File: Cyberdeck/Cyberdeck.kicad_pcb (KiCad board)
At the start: 4 copper layers, 66 parts, among them SW1 Slide Switch, SW10 Push Button, SW11 Push Button, SW2 Push Button, SW3 Push Button, SW4 Push Button, SW5 Push Button, SW6 Push Button, SW7 Push Button, SW8 Push Button, SW9 Push Button, U1 18650 Positive Clip, U2 BQ24075 Charger, U3 0.47uH, U4 TPS62827 Regulator, U5 STM32F411CEU6, X1 32.768KHz 12.5pF, X2 25MHZ 12PF 10PPM

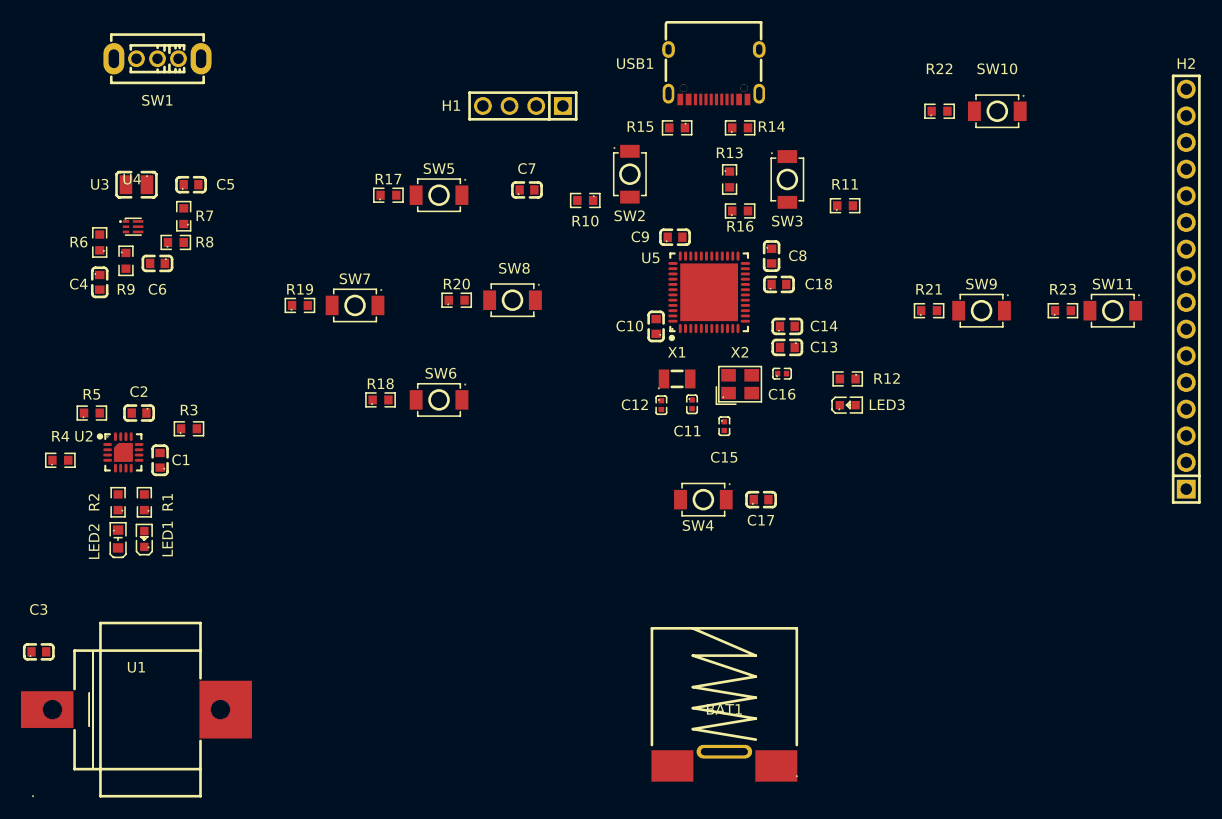
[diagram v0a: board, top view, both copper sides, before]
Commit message: Optimized component placement
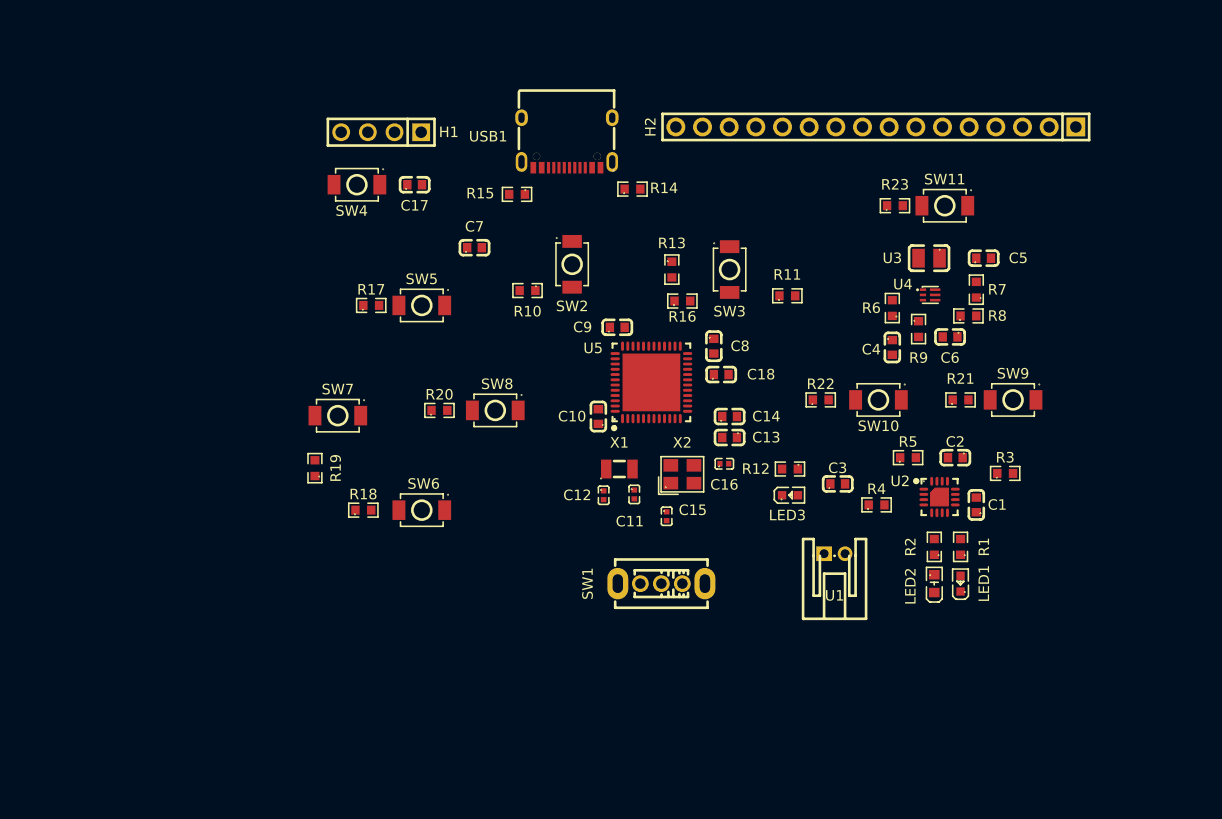
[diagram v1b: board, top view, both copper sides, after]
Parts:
- removed BAT1: 18650 Neg Clip, lcsc_footprints:C19184124_BAT-TH_MY-18650-05-J
- U1: value 18650 Positive Clip -> JST-PH BAT; footprint lcsc_footprints:C2979182_BAT-SMD_MY-18650-02 -> lcsc_footprints:C173752_CONN-TH_S2B-PH-K-S-LF-SN
- moved C1 77.9 mm to (181.5, 110.0)
- moved C2 77.9 mm to (179.5, 105.5)
- moved LED1 77.9 mm to (180.0, 117.5)
- moved LED2 77.9 mm to (177.5, 117.5)
- moved R1 77.9 mm to (180.0, 114.0)
- moved R2 77.9 mm to (177.5, 114.0)
- moved R3 77.9 mm to (184.2, 107.0)
- moved R4 77.9 mm to (172.0, 110.0)
- moved R5 77.9 mm to (175.0, 105.5)
- moved U2 77.9 mm to (178.0, 109.2)
- moved C3 77.8 mm to (168.3, 108.0)
- moved U4 76.2 mm to (177.0, 90.0)
- moved C6 75.8 mm to (179.0, 94.0)
- moved R7 75.8 mm to (181.5, 89.5)
- moved R8 75.8 mm to (180.8, 92.0)
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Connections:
- U1 pad 1: /V_BAT -> GND

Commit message: Routed all connections
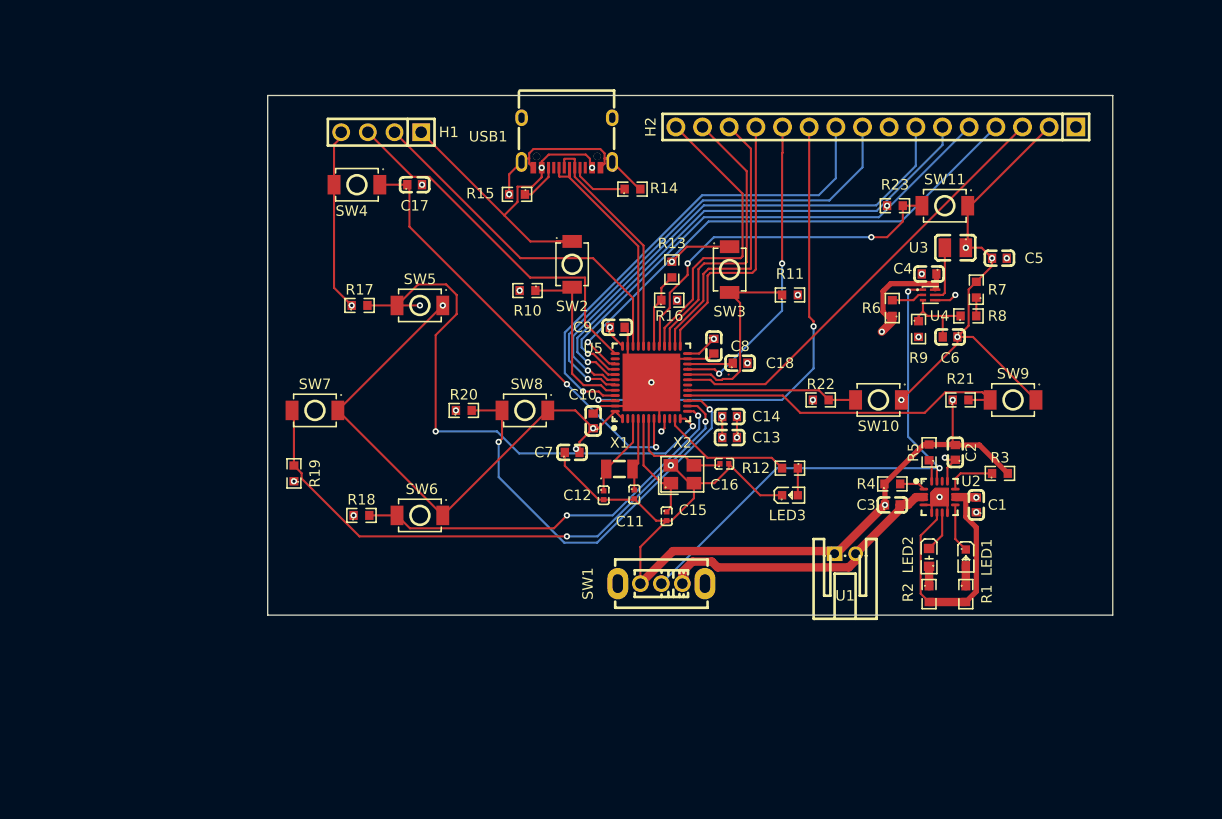
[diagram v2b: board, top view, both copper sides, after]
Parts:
- moved C7 21.6 mm to (143.0, 105.0)
- moved C4 7.83 mm to (177.0, 88.0), turned to 180 degrees
- moved C3 5.57 mm to (173.5, 110.0)
- moved R1 4.53 mm to (180.5, 118.5), turned to -90 degrees
- moved R2 4.53 mm to (177.0, 118.5), turned to -90 degrees
- moved SW8 2.82 mm to (138.5, 101.0)
- moved U3 2.69 mm to (179.5, 85.5)
- moved LED1 2.55 mm to (180.5, 115.0), turned to -90 degrees
- moved LED2 2.55 mm to (177.0, 115.0), turned to 90 degrees
- moved R4 2.50 mm to (173.5, 108.0)
- moved R20 2.32 mm to (132.7, 101.0)
- moved SW7 2.24 mm to (118.5, 101.0)
- moved C18 2.10 mm to (159.0, 96.5)
- moved R19 2.06 mm to (116.5, 107.0)
- moved R5 2.06 mm to (177.0, 105.0), turned to 90 degrees
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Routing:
- net GND: track 0.00 -> 468.2 mm, vias 0 -> 24
- net /V_IN: track 0.00 -> 334.7 mm, vias 0 -> 16
- net /V_CHG: track 0.00 -> 59.9 mm, vias 0 -> 2
- net /LEFT: track 0.00 -> 55.3 mm, vias 0 -> 2
- net /UP: track 0.00 -> 53.7 mm, vias 0 -> 3
- net /Switch: track 0.00 -> 52.0 mm, vias 0 -> 2
- net /C/D: track 0.00 -> 50.8 mm, vias 0 -> 1
- net /WR: track 0.00 -> 50.1 mm, vias 0 -> 1
- net /RD: track 0.00 -> 50.0 mm, vias 0 -> 1
- net /RST: track 0.00 -> 49.9 mm, vias 0 -> 1
- net /D2: track 0.00 -> 46.6 mm, vias 0 -> 2
- net /D1: track 0.00 -> 46.3 mm, vias 0 -> 1
- net /D0: track 0.00 -> 46.3 mm, vias 0 -> 1
- net /CS: track 0.00 -> 42.2 mm
- net /MicroController/NRST: track 0.00 -> 41.7 mm, vias 0 -> 2
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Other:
- board outline added: 80.5 x 49.5 mm

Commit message: Rerouted vias, optimized layout, and added pwr/gnd planes
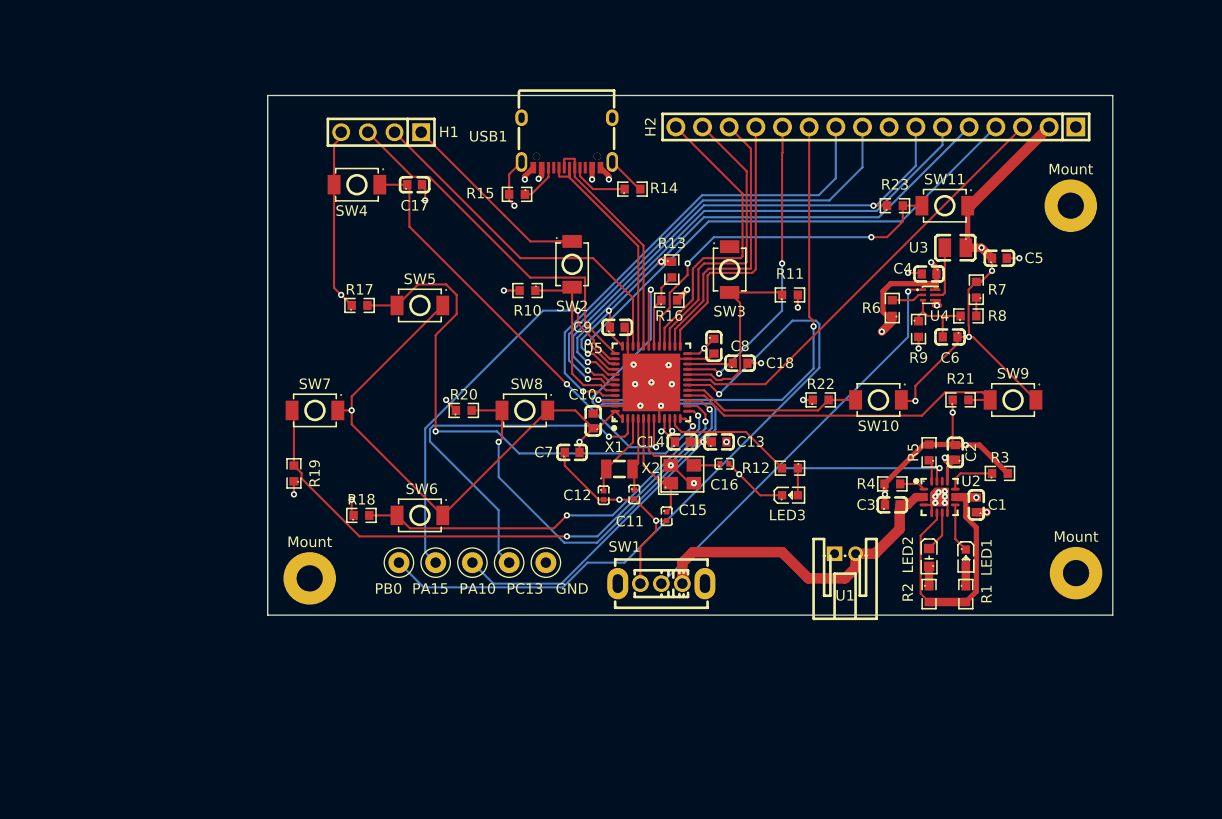
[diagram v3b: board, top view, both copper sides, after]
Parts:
- added GND: TestPoint, TestPoint:TestPoint_Keystone_5000-5004_Miniature, F.Cu at (140.5, 115.5)
- added Mount: MountingHole, MountingHole:MountingHole_2.5mm_Pad, F.Cu at (118.0, 117.0)
- added Mount: MountingHole, MountingHole:MountingHole_2.5mm_Pad, F.Cu at (191.0, 116.5)
- added Mount: MountingHole, MountingHole:MountingHole_2.5mm_Pad, F.Cu at (190.5, 81.5)
- added PA10: TestPoint, TestPoint:TestPoint_Keystone_5000-5004_Miniature, F.Cu at (133.5, 115.5)
- added PA15: TestPoint, TestPoint:TestPoint_Keystone_5000-5004_Miniature, F.Cu at (130.0, 115.5)
- added PB0: TestPoint, TestPoint:TestPoint_Keystone_5000-5004_Miniature, F.Cu at (126.5, 115.5)
- added PC13: TestPoint, TestPoint:TestPoint_Keystone_5000-5004_Miniature, F.Cu at (137.0, 115.5)
- moved C14 5.11 mm to (153.5, 104.0)
- moved C13 1.08 mm to (157.0, 104.0), turned to 0 degrees
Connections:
- C10 pad 1: /V_IN -> /V_REG
- C13 pad 2: /V_IN -> /V_REG
- C14 pad 1: /V_IN -> /V_REG
- C2 pad 1: /V_IN -> /V_USB
- C5 pad 1: /V_IN -> /V_REG
- C6 pad 1: /V_IN -> /V_REG
- C7 pad 2: /V_IN -> /V_REG
- C8 pad 1: /V_IN -> /V_REG
- C9 pad 1: /V_IN -> /V_REG
- H1 pad 1: /V_IN -> /V_REG
- H2 pad 2: /V_IN -> /V_REG
- R13 pad 1: /V_IN -> /V_USB
- R7 pad 2: /V_IN -> /V_REG
- SW1 pad 4: unconnected-(SW1-Pad4) -> GND
- SW1 pad 5: unconnected-(SW1-Pad5) -> GND
- SW10 pad 2: /V_IN -> /V_REG
- SW11 pad 2: /V_IN -> /V_REG
- SW2 pad 2: /V_IN -> /V_REG
- SW3 pad 2: /V_IN -> /V_REG
- SW5 pad 2: /V_IN -> /V_REG
- SW6 pad 2: /V_IN -> /V_REG
- SW7 pad 2: /V_IN -> /V_REG
- SW8 pad 2: /V_IN -> /V_REG
- SW9 pad 2: /V_IN -> /V_REG
- U2 pad 13: /V_IN -> /V_USB
- U3 pad 1: /V_IN -> /V_REG
- U5 pad 1: /V_IN -> /V_REG
- U5 pad 24: /V_IN -> /V_REG
- U5 pad 36: /V_IN -> /V_REG
- U5 pad 48: /V_IN -> /V_REG
- U5 pad 9: /V_IN -> /V_REG
- USB1 pad A4B9: /V_IN -> /V_USB
- USB1 pad B4A9: /V_IN -> /V_USB
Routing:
- net /V_IN: track 334.7 -> 0.00 mm, vias 16 -> 0
- net GND: track 468.2 -> 142.1 mm, vias 24 -> 41
- net /V_REG: track 0.00 -> 130.0 mm, vias 0 -> 10
- net /V_USB: track 0.00 -> 114.9 mm, vias 0 -> 4
- net /MicroController/PB0: track 0.00 -> 69.8 mm, vias 0 -> 1
- net /MicroController/PA10: track 0.00 -> 62.7 mm, vias 0 -> 1
- net /MicroController/PA15: track 0.00 -> 38.7 mm, vias 0 -> 1
- net /MicroController/PC13: track 0.00 -> 36.8 mm, vias 0 -> 1
- net /Switch: track 52.0 -> 55.9 mm
- net /V_BAT: track 32.1 -> 35.7 mm
- net /UP: track 53.7 -> 51.5 mm, vias 3 -> 2
- net /MicroController/PA0: track 0.00 -> 1.28 mm, vias 0 -> 1
- net /V_CHG: track 59.9 -> 60.8 mm, vias 2 -> 3
- net /B_SELECT: track 16.4 -> 17.3 mm
- added copper zone on In2.Cu, net /V_REG
- added copper zone on In1.Cu, net GND

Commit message: Resolved DRC
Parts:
- added PA0: TestPoint, TestPoint:TestPoint_Keystone_5000-5004_Miniature, F.Cu at (123.0, 115.5)
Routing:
- net /MicroController/PA0: track 1.28 -> 58.0 mm, vias 1 -> 2
- net /MicroController/PC13: track 36.8 -> 39.0 mm
- net /MicroController/PA15: track 38.7 -> 40.8 mm
- net /V_CHG: track 60.8 -> 59.5 mm, vias 3 -> 2
- net /UP: track 51.5 -> 52.3 mm
- net /V_REG: track 130.0 -> 130.2 mm, vias 10 -> 11
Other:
- board text added: "Adam Kollgaard - Cyberdeck V1 10/2026"

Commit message: Finalized PCB; Made gerber files
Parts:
- added 3V3: TestPoint, TestPoint:TestPoint_Keystone_5000-5004_Miniature, F.Cu at (161.5, 115.4)
- added D1: ESD321, lcsc_footprints:C2868952_X1SON-2_L1_0-W0_6-P0_65-RD-1, F.Cu at (142.2, 80.2)
- added D2: ESD321, lcsc_footprints:C2868952_X1SON-2_L1_0-W0_6-P0_65-RD-1, F.Cu at (147.4, 81.3)
- added D3: ESDA7P60, lcsc_footprints:C1975146_D1610-RD, F.Cu at (151.9, 78.0)
- C10, C14, C17, C8, C9: footprint lcsc_footprints:C1591_C0603 -> lcsc_footprints:C66501_C0603
- moved Mount 1.40 mm to (189.6, 116.4)
- moved C9 0.99 mm to (148.1, 92.5), turned to 90 degrees
- moved C10 0.22 mm to (145.2, 102.1), turned to -90 degrees
- moved C8 0.15 mm to (156.6, 95.0), turned to 90 degrees
- moved C14 0.14 mm to (153.6, 104.1), turned to 180 degrees
- moved C17 0.10 mm to (128.0, 79.6), turned to 180 degrees
- renumbered R14 to R13, R15 to R14, R13 to R15
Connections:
- C10 pad 1: /V_REG -> GND
- C10 pad 2: GND -> /V_REG
- C14 pad 1: /V_REG -> GND
- C14 pad 2: GND -> /V_REG
- C17 pad 1: /MicroController/NRST -> GND
- C17 pad 2: GND -> /MicroController/NRST
- C8 pad 1: /V_REG -> GND
- C8 pad 2: GND -> /V_REG
- C9 pad 1: /V_REG -> GND
- C9 pad 2: GND -> /V_REG
- SW1 pad 1: /V_BAT -> /V_CHG
- U2 pad 15: /Switch -> GND
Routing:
- net /V_CHG: track 59.5 -> 85.4 mm
- net /V_BAT: track 35.7 -> 13.1 mm
- net /Switch: track 55.9 -> 39.1 mm, vias 2 -> 1
- net /V_USB: track 114.9 -> 117.5 mm, vias 4 -> 5
- net GND: track 142.1 -> 144.6 mm, vias 41 -> 36
- net /D2: track 46.6 -> 44.6 mm
- net /V_REG: track 130.2 -> 131.8 mm
- net /MicroController/DN: track 22.4 -> 23.6 mm
- net /MicroController/PA10: track 62.7 -> 64.0 mm
- net /MicroController/DP: track 22.4 -> 23.5 mm
- net /MicroController/PB0: track 69.8 -> 68.8 mm
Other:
- board size 80.5 x 49.5 mm -> 80 x 50 mm
- board text added: "+"
- board text added: "-"
- board text added: "CHARGING"
- board text added: "PGOOD"
